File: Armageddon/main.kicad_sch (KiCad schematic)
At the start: 0 parts

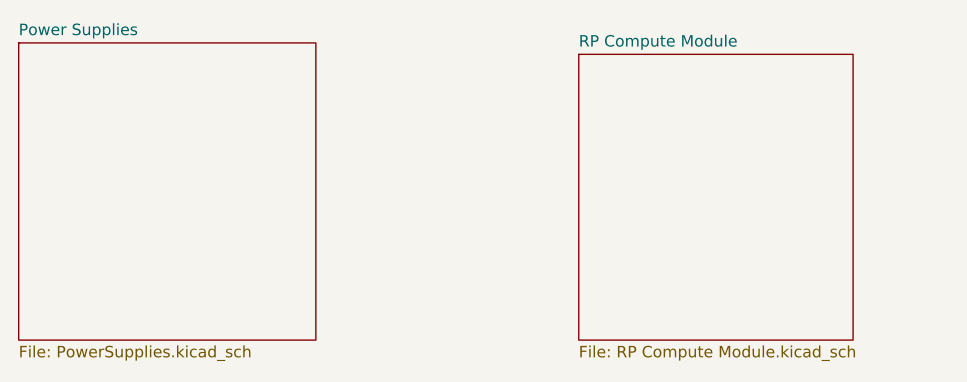
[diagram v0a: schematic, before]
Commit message: Updated Molex USB C Symbol
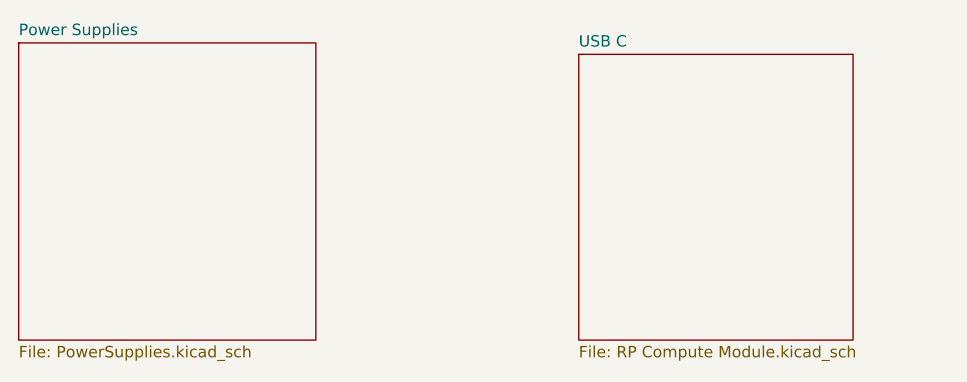
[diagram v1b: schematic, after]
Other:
- sheet RP Compute Module renamed USB C
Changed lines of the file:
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@@
 			(color 0 0 0 0)
 		)
-		(property "Sheetname" "RP Compute Module"
+		(property "Sheetname" "USB C"
 			(at 92.71 29.7684 0)
 			(show_name no)
